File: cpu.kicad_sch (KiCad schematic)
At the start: 23 parts, among them IC1 68HC000, IC2 LHP6323, IC7 MSM54C864

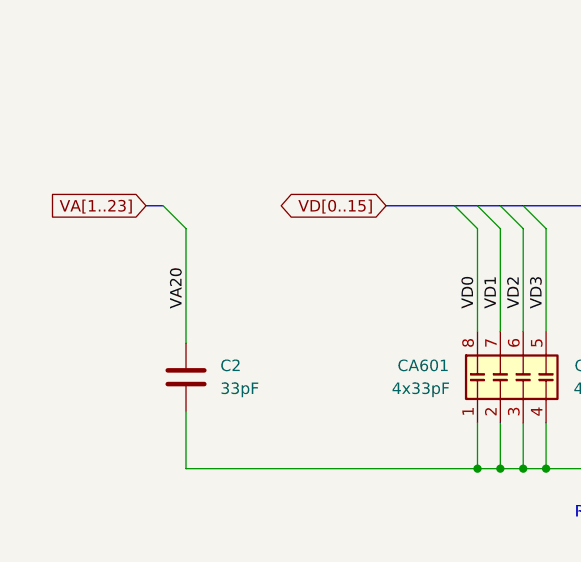
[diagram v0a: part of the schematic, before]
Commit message: Correct connection of C2 to VA21 (issue #12).
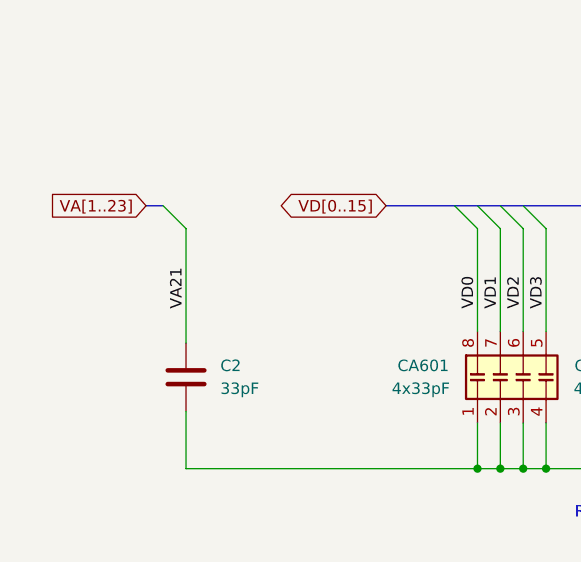
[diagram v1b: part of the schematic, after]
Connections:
- net VA20: no longer C2.1
- net VA21: now also C2.1
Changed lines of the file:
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@@
 		)
 	)
-	(label "VA20"
+	(label "VA21"
 		(at 65.405 223.52 90)
 		(effects
